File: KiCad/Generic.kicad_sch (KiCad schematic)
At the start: 39 parts, among them J1 Connector, J2 USB-C, J3 DC, U1 ESP32-WROOM-32, U2 FT231XQ, U3 LMR16006+FB

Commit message: Various minor tidy
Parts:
- J2: symbol Connector:USB_C_Receptacle_USB2.0 -> RevK:USB-C
- J3: footprint Connector_PinHeader_2.54mm:PinHeader_1x02_P2.54mm_Vertical -> RevK:Molex_MiniSPOX_H2RA
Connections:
- no-connect marks 18 -> 16
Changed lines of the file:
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@@
   (junction (at 85.725 152.4) (diameter 0) (color 0 0 0 0)
   )
-  (junction (at 170.815 43.18) (diameter 0) (color 0 0 0 0)
-  )
   (junction (at 90.805 157.48) (diameter 0) (color 0 0 0 0)
   )
@@
   )
   (junction (at 85.725 137.16) (diameter 0) (color 0 0 0 0)
-  )
-  (junction (at 170.815 40.64) (diameter 0) (color 0 0 0 0)
   )
   (no_connect (at 80.645 74.93))
   (no_connect (at 80.645 82.55))
-  (no_connect (at 170.815 53.34))
   (no_connect (at 50.165 80.01))
   (no_connect (at 50.165 74.93))
@@
   (no_connect (at 50.165 72.39))
   (no_connect (at 185.42 129.54))
-  (no_connect (at 170.815 55.88))
   (no_connect (at 80.645 77.47))
   (no_connect (at 50.165 77.47))
@@
     (stroke (width 0) (type default) (color 0 0 0 0))
   )
-  (wire (pts (xy 170.815 38.1) (xy 170.815 40.64))
-    (stroke (width 0) (type default) (color 0 0 0 0))
-  )
   (wire (pts (xy 177.8 63.5) (xy 183.515 63.5))
     (stroke (width 0) (type default) (color 0 0 0 0))
@@
   )
   (wire (pts (xy 66.675 157.48) (xy 90.805 157.48))
-    (stroke (width 0) (type default) (color 0 0 0 0))
-  )
-  (wire (pts (xy 170.815 45.72) (xy 170.815 43.18))
     (stroke (width 0) (type default) (color 0 0 0 0))
   )
@@
       (effects (font (size 1.27 1.27)) (justify right))
     )
-    (property "Footprint" "Connector_PinHeader_2.54mm:PinHeader_1x02_P2.54mm_Vertical" (id 2) (at 238.125 46.355 0)
+    (property "Footprint" "RevK:Molex_MiniSPOX_H2RA" (id 2) (at 238.125 46.355 0)
       (effects (font (size 1.27 1.27)) hide)
     )
@@
     (pin "2")
   )
-  (symbol (lib_id "Connector:USB_C_Receptacle_USB2.0") (at 155.575 40.64 0) (unit 1)
+  (symbol (lib_id "RevK:USB-C") (at 155.575 40.64 0) (unit 1)
     (in_bom yes) (on_board yes)
     (property "Reference" "J2" (id 0) (at 158.2928 18.6182 0))
     (property "Value" "USB-C" (id 1) (at 158.2928 20.9296 0))
-    (property "Footprint" "RevK:USC16-TR-Round" (id 2) (at 159.385 40.64 0)
-      (effects (font (size 1.27 1.27)) hide)
-    )
-    (property "Datasheet" "https://www.usb.org/sites/default/files/documents/usb_type-c.zip" (id 3) (at 159.385 40.64 0)
+    (property "Footprint" "RevK:USC16-TR-Round" (id 2) (at 155.575 20.32 0)
+      (effects (font (size 1.27 1.27)) hide)
+    )
+    (property "Datasheet" "https://www.usb.org/sites/default/files/documents/usb_type-c.zip" (id 3) (at 155.575 17.78 0)
       (effects (font (size 1.27 1.27)) hide)
     )
@@
     )
     (path "/00000000-0000-0000-0000-000060460b50"
-      (reference "J3") (unit 1) (value "DC") (footprint "Connector_PinHeader_2.54mm:PinHeader_1x02_P2.54mm_Vertical")
+      (reference "J3") (unit 1) (value "DC") (footprint "RevK:Molex_MiniSPOX_H2RA")
     )
     (path "/00000000-0000-0000-0000-0000610fe01a"

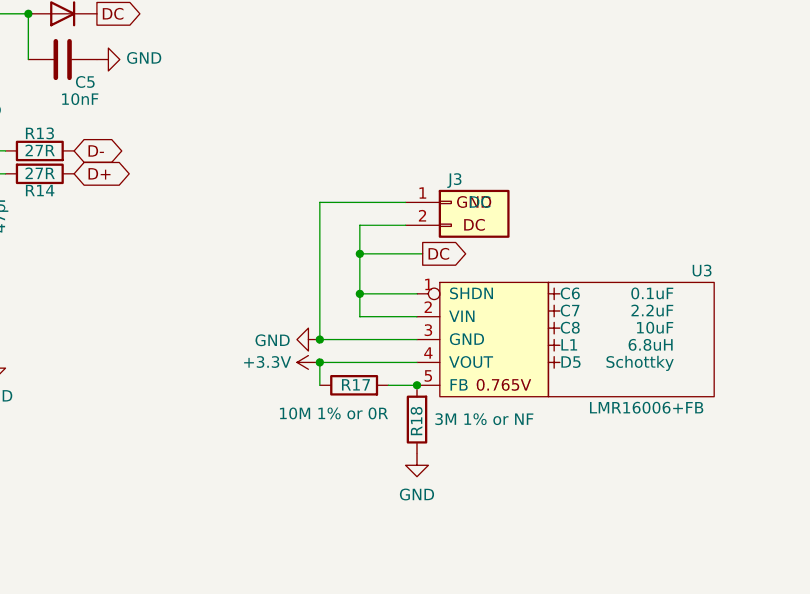
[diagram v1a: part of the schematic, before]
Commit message: Change resistor values
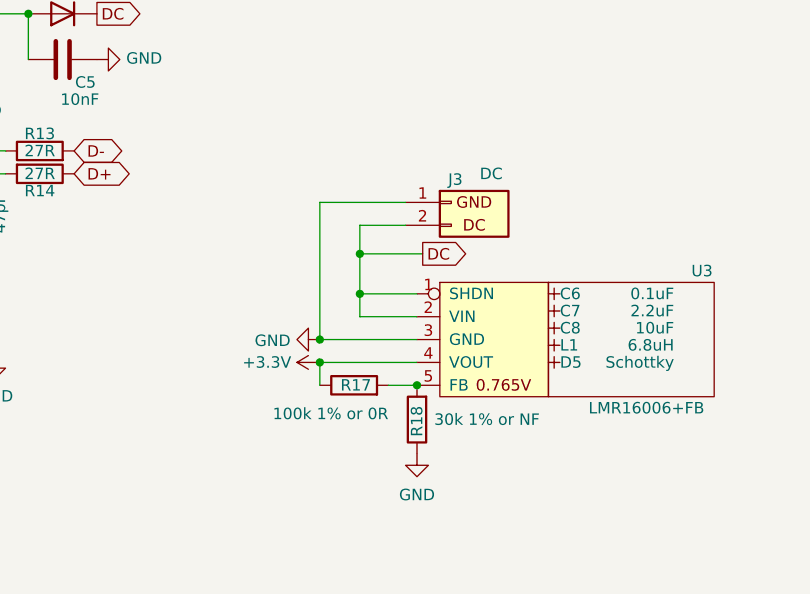
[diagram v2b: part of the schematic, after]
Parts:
- J3: footprint RevK:Molex_MiniSPOX_H2RA -> RevK:DC
- R17: value 10M 1% or 0R -> 100k 1% or 0R
- R18: value 3M 1% or NF -> 30k 1% or NF
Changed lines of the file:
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@@
       (effects (font (size 1.27 1.27)) (justify right))
     )
-    (property "Value" "DC" (id 1) (at 242.57 46.355 0)
-      (effects (font (size 1.27 1.27)) (justify right))
-    )
-    (property "Footprint" "RevK:Molex_MiniSPOX_H2RA" (id 2) (at 238.125 46.355 0)
+    (property "Value" "DC" (id 1) (at 243.84 43.18 0)
+      (effects (font (size 1.27 1.27)) (justify right))
+    )
+    (property "Footprint" "RevK:DC" (id 2) (at 238.125 46.355 0)
       (effects (font (size 1.27 1.27)) hide)
     )
@@
       (effects (font (size 1.27 1.27)) (justify right))
     )
-    (property "Value" "3M 1% or NF" (id 1) (at 236.22 70.485 0)
+    (property "Value" "30k 1% or NF" (id 1) (at 236.22 70.485 0)
       (effects (font (size 1.27 1.27)) (justify right))
     )
@@
       (effects (font (size 1.27 1.27)) (justify left))
     )
-    (property "Value" "10M 1% or 0R" (id 1) (at 231.14 69.85 90)
+    (property "Value" "100k 1% or 0R" (id 1) (at 231.14 69.85 90)
       (effects (font (size 1.27 1.27)) (justify left))
     )
@@
     )
     (path "/00000000-0000-0000-0000-000060460b50"
-      (reference "J3") (unit 1) (value "DC") (footprint "RevK:Molex_MiniSPOX_H2RA")
+      (reference "J3") (unit 1) (value "DC") (footprint "RevK:DC")
     )
     (path "/00000000-0000-0000-0000-0000610fe01a"
@@
     )
     (path "/fc3ca677-79f2-42b6-a5b3-ff3b18df1d6c"
-      (reference "R17") (unit 1) (value "10M 1% or 0R") (footprint "RevK:R_0603")
+      (reference "R17") (unit 1) (value "100k 1% or 0R") (footprint "RevK:R_0603")
     )
     (path "/83151023-5106-4495-aeff-aefc75dfd6c0"
-      (reference "R18") (unit 1) (value "3M 1% or NF") (footprint "RevK:R_0603")
+      (reference "R18") (unit 1) (value "30k 1% or NF") (footprint "RevK:R_0603")
     )
     (path "/d3737146-f8f2-4cf9-a53d-a4805b531c09"
